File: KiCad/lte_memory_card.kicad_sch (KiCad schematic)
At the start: 20 parts, among them J1 Conn_02x30_Odd_Even, U1 MCM414256, U10 MCM414256, U11 MCM414256, U12 MCM414256, U13 MCM414256, U14 MCM414256, U15 MCM414256, U16 MCM414256, U2 MCM414256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

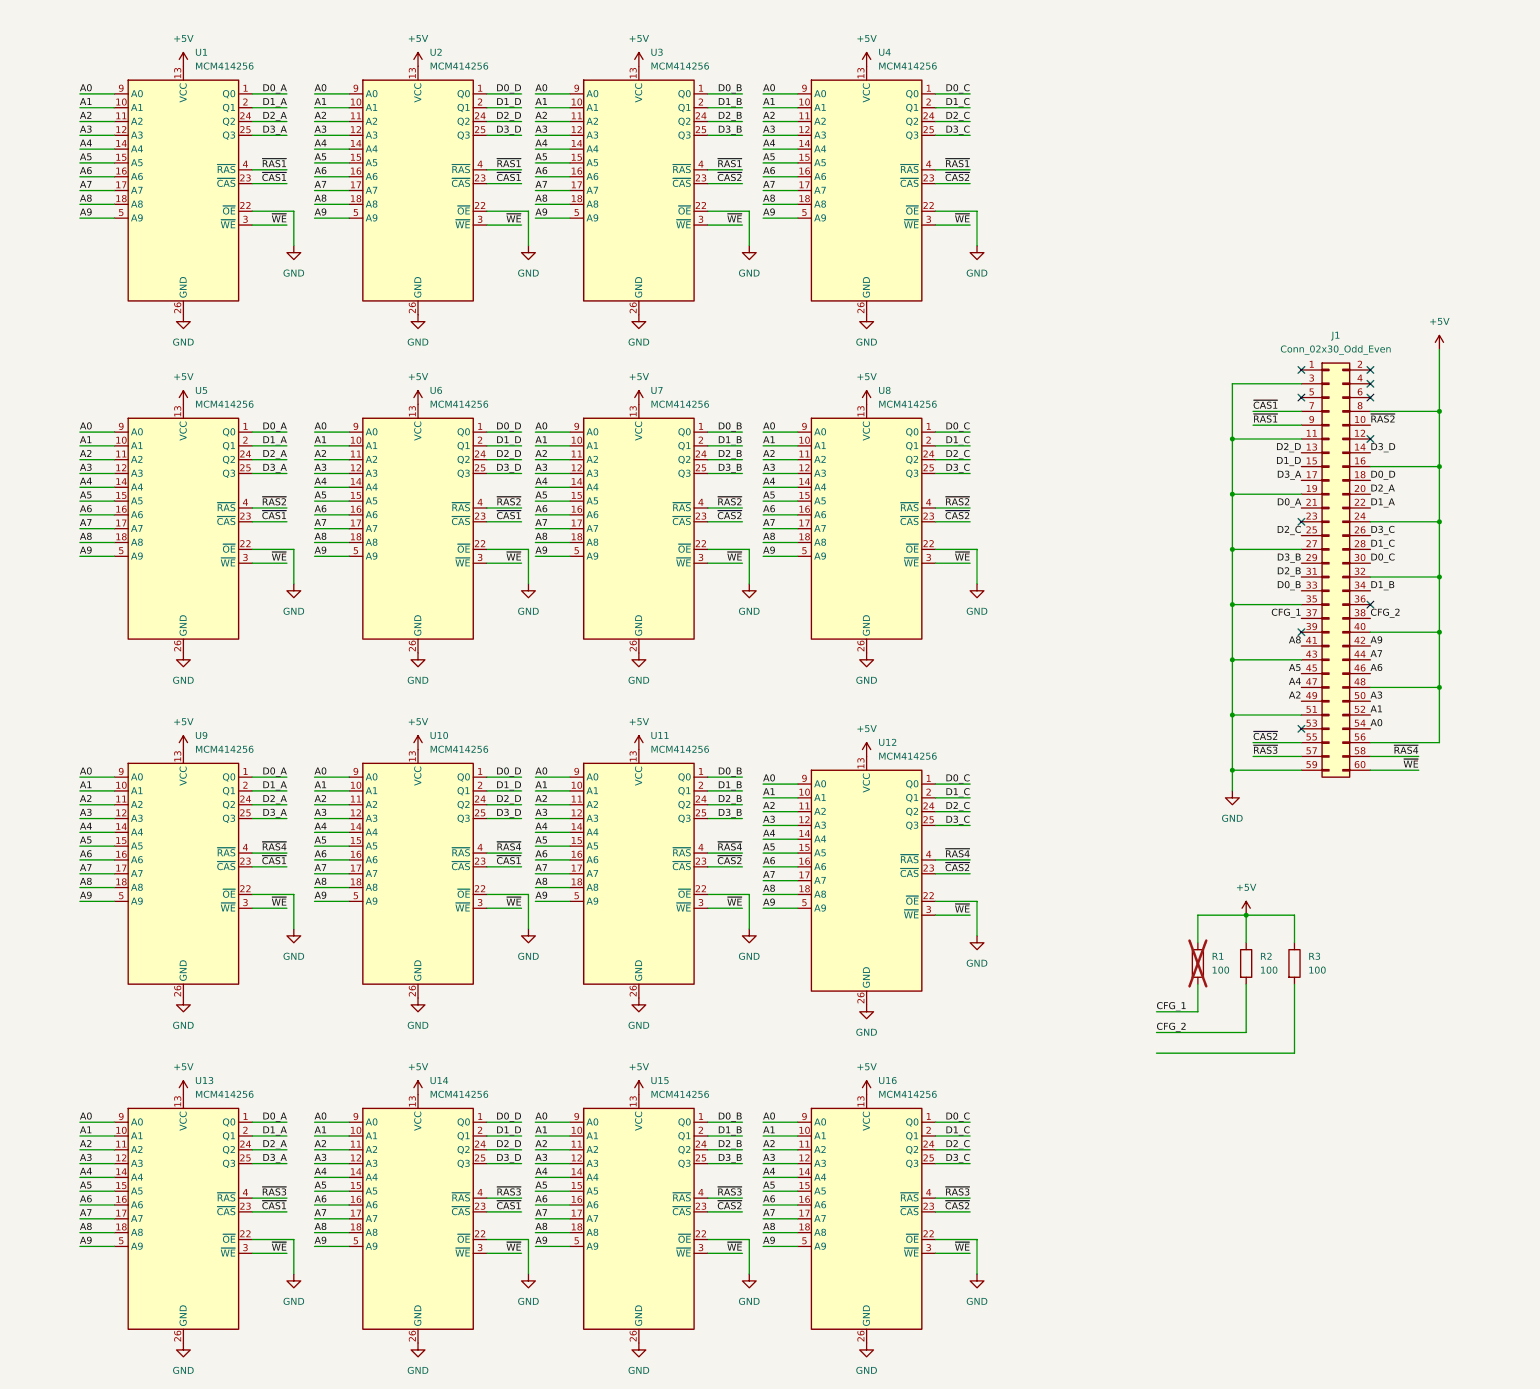
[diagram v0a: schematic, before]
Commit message: added 'ringing' resistor to A9
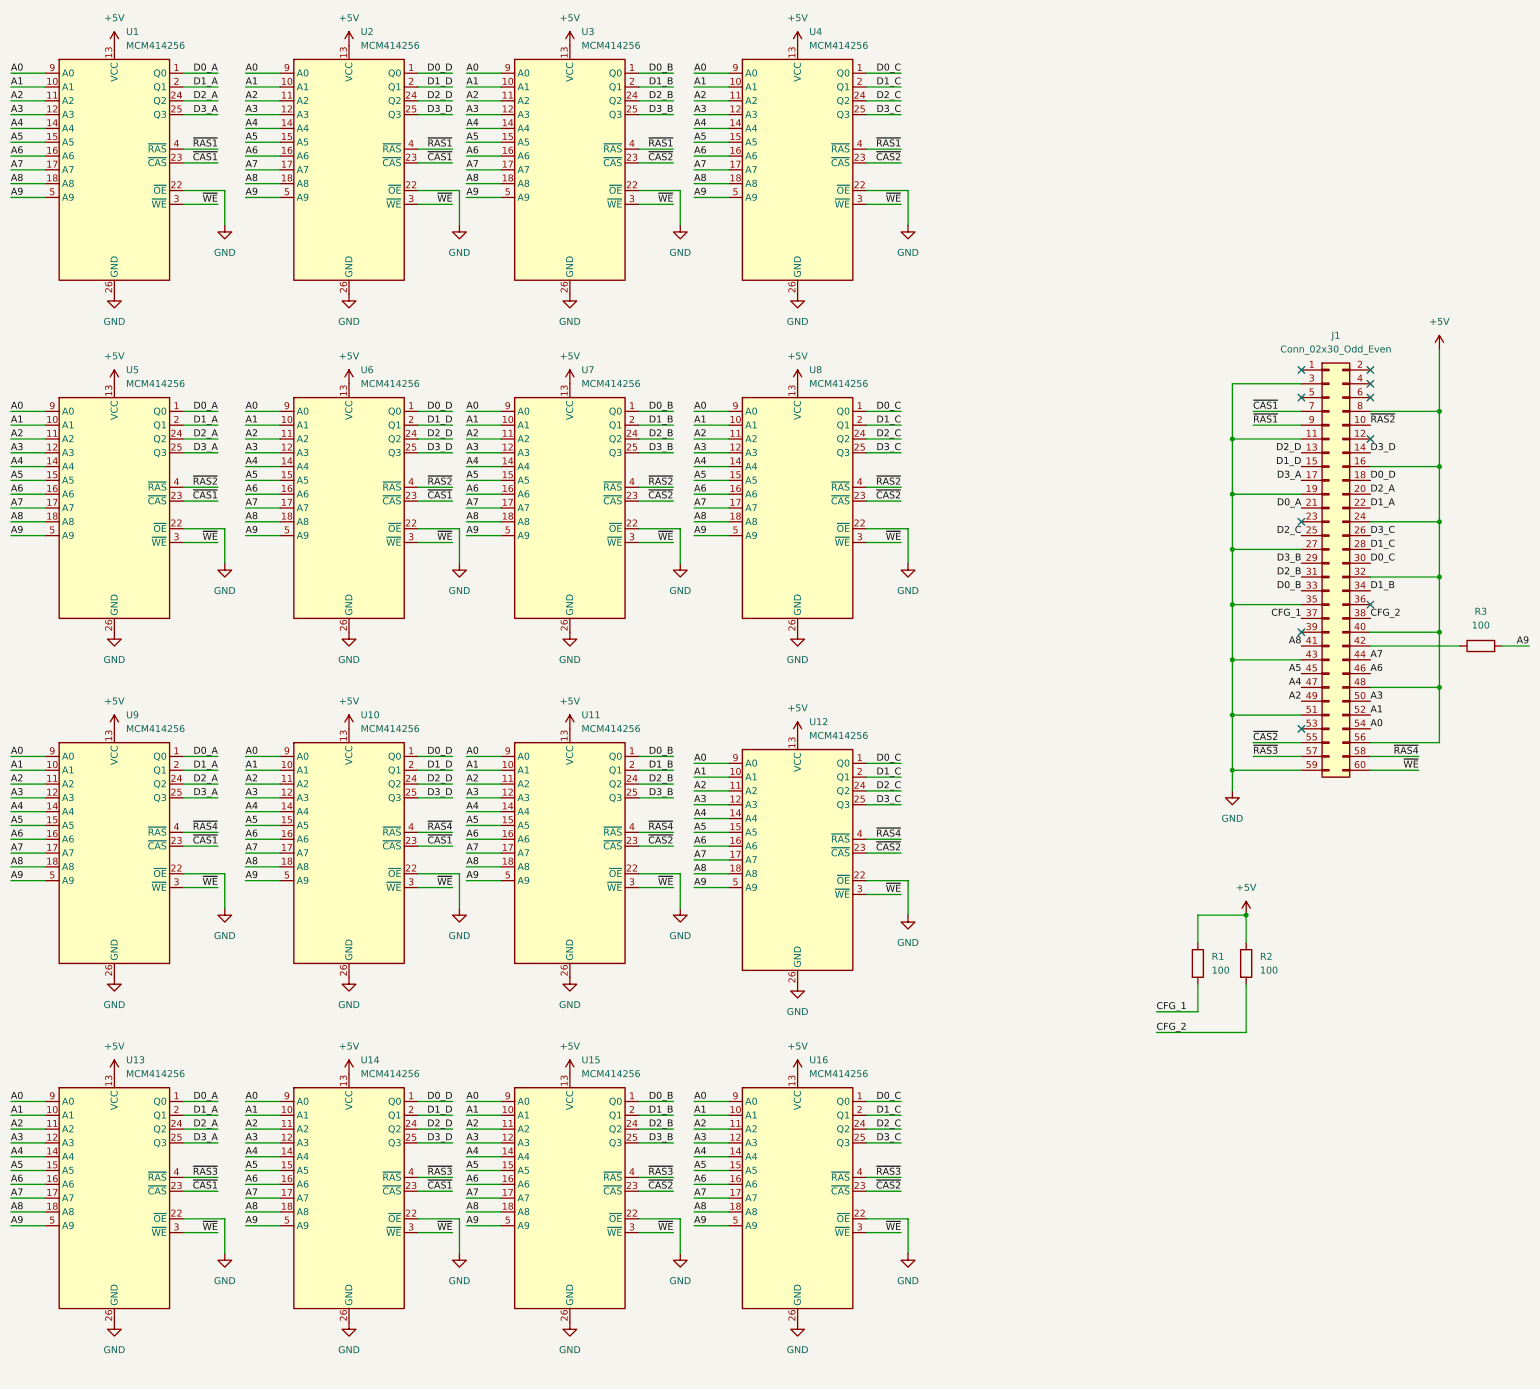
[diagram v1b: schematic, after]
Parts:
- R1: now fitted
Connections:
- net +5V: no longer R3.1
- net A9: now also R3.2; no longer J1.42 (Pin_42)
- new net: J1.42 (Pin_42), R3.1
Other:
- moved on the sheet: R3, U1, U10, U11, U12, U13, U14, U15, U16, U2, U3, U4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

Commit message: config resistor analysis
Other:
- note added: "Not sure if these are tied to +5V or GND. For now I believe CFG_1 enables RAS2 and RAS4 and R2 enables RAS1 and RAS3."
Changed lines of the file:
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@@
 	(generator_version "9.0")
 	(paper "A3")
+	(rectangle
+		(start 212.09 182.88)
+		(end 295.91 226.06)
+		(stroke
+			(width 0)
+			(type default)
+		)
+		(fill
+			(type none)
+		)
+	)
+	(text "Not sure if these are tied to +5V or GND.\n\nFor now I believe CFG_1 enables RAS2 and RAS4 and R2 enables RAS1 and RAS3."
+		(exclude_from_sim no)
+		(at 253.746 219.964 0)
+		(effects
+			(font
+				(size 1.27 1.27)
+			)
+		)
+	)
 	(junction
 		(at 254 114.3)

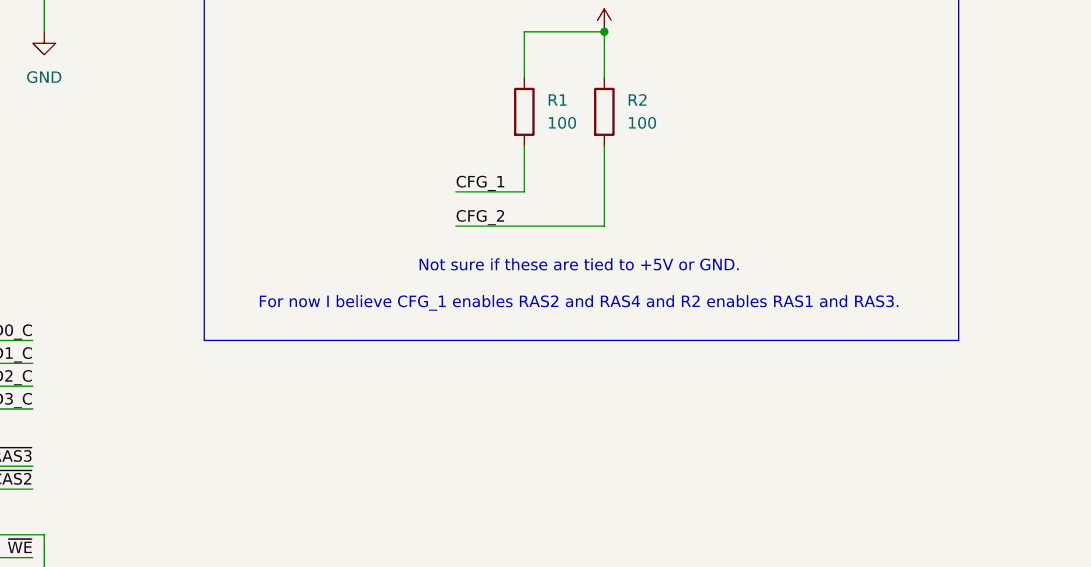
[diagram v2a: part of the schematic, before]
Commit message: further analysis on config resistors
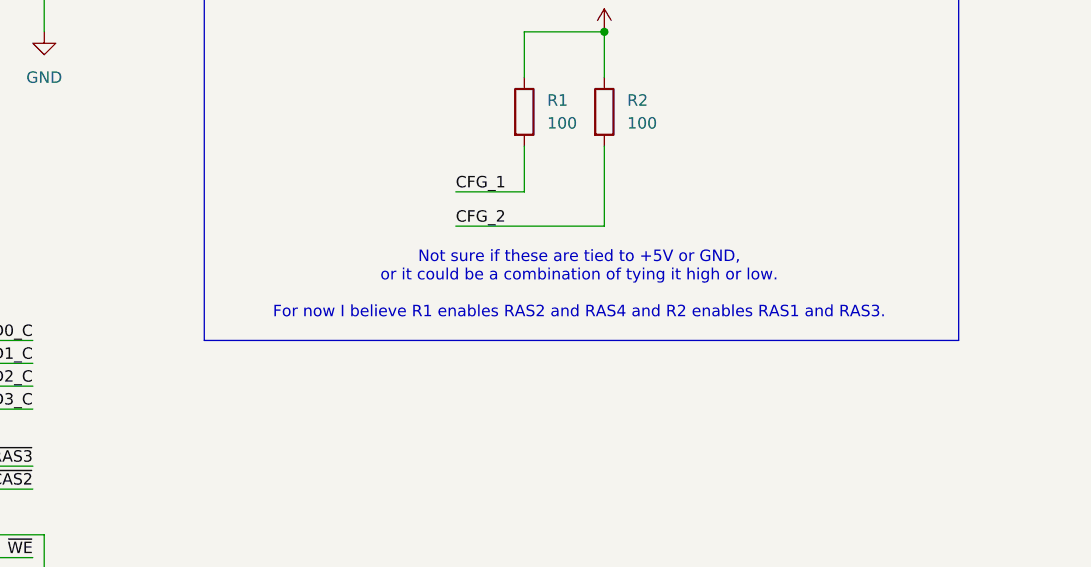
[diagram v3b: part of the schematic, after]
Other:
- note added: "Not sure if these are tied to +5V or GND, or it could be a combination of tying it high or low. For now I believe R1 enables RAS2 and RAS4 and R2 enables RAS1 and RAS3."
- note removed: "Not sure if these are tied to +5V or GND. For now I believe CFG_1 enables RAS2 and RAS4 and R2 enables RAS1 and RAS3."
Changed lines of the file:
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@@
 		)
 	)
-	(text "Not sure if these are tied to +5V or GND.\n\nFor now I believe CFG_1 enables RAS2 and RAS4 and R2 enables RAS1 and RAS3."
+	(text "Not sure if these are tied to +5V or GND, \nor it could be a combination of tying it high or low.\n\nFor now I believe R1 enables RAS2 and RAS4 and R2 enables RAS1 and RAS3."
 		(exclude_from_sim no)
 		(at 253.746 219.964 0)
